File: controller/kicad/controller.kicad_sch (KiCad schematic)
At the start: 33 parts, among them J1 pcie_98, J2 USB_C_Receptacle_USB2.0, U1 WeAct_STM32H750_Module, U10 ESD5344D, U11 ESD5344D, U12 ESD5344D, U13 ESD5344D, U14 ESD5344D, U15 ESD5344D, U16 CP2102N-A01-GQFN28-Interface_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, U2 ESD5344D, U3 ESD5344D, U4 ESD5344D, U5 ESD5344D, U6 ESD5344D, U7 ESD5344D, U8 ESD5344D, U9 ESD5344D

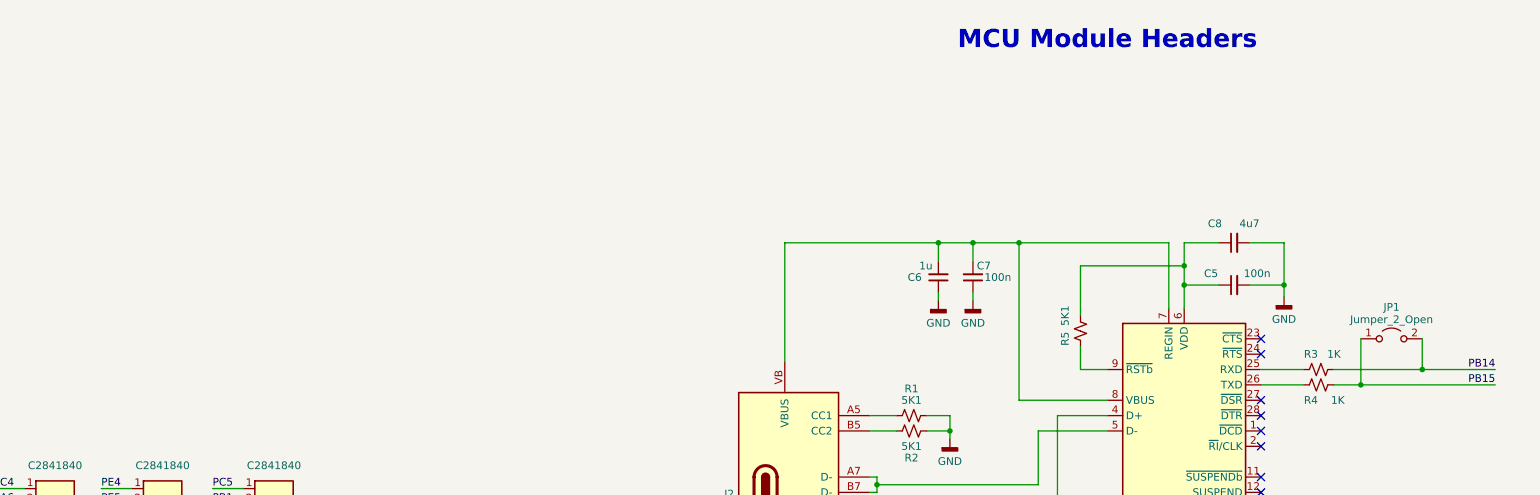
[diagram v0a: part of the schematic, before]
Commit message: Updated the Controller's schematic to reflect the new RX/TX pin of the datalink serial link.
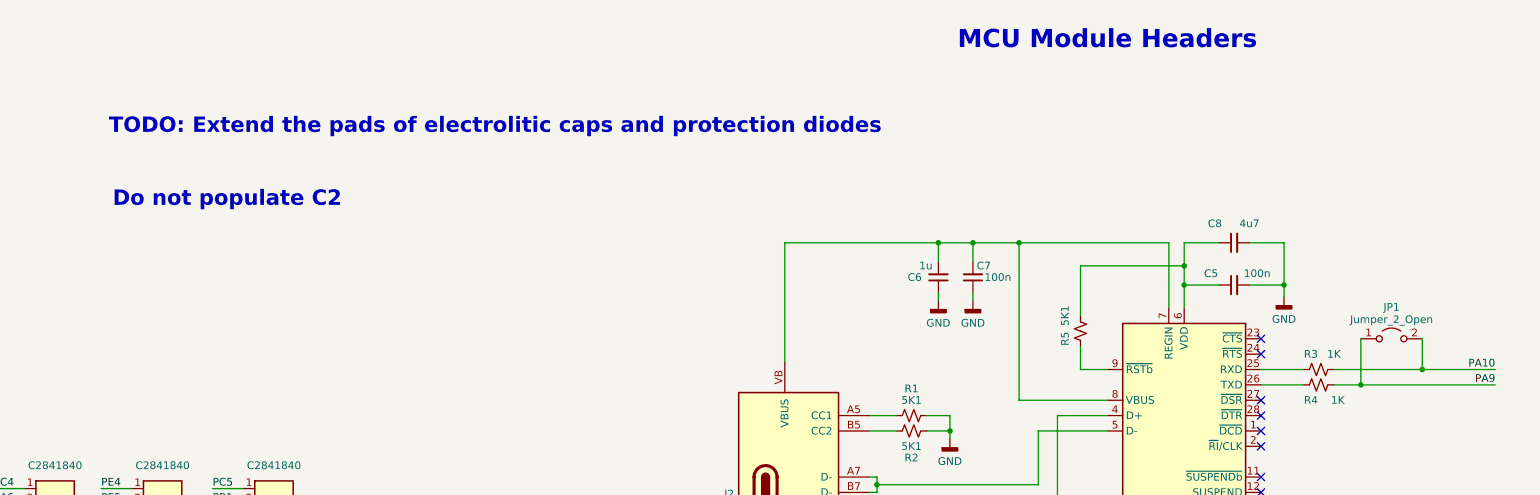
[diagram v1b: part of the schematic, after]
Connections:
- net PA10: now also JP1.2 (B), R3.2
- net PA9: now also JP1.1 (A), R4.2
- net PB14: no longer JP1.2 (B), R3.2
- net PB15: no longer JP1.1 (A), R4.2
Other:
- note added: "Do not populate C2"
- note added: "TODO: Extend the pads of electrolitic caps and protection diodes"
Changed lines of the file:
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@@
     (effects (font (size 3 3) (thickness 0.6) bold) (justify left bottom))
+  )
+  (text "TODO: Extend the pads of electrolitic caps and protection diodes"
+    (at 138.43 140.335 0)
+    (effects (font (size 2.54 2.54) (thickness 0.508) bold (color 255 0 0 1)) (justify left bottom))
   )
   (text "MCU Module Headers" (at 278.765 126.365 0)
@@
   (text "Edge Connector" (at 32.385 105.41 0)
     (effects (font (size 3 3) (thickness 0.6) bold) (justify left bottom))
+  )
+  (text "Do not populate C2" (at 139.065 152.4 0)
+    (effects (font (size 2.54 2.54) (thickness 0.508) bold (color 255 0 0 1)) (justify left bottom))
   )
   (text "POWER" (at 170.18 106.68 0)
@@
     (effects (font (size 1.27 1.27)) (justify left bottom))
   )
-  (label "PB15" (at 367.665 181.61 180) (fields_autoplaced)
+  (label "PA9" (at 367.665 181.61 180) (fields_autoplaced)
     (effects (font (size 1.27 1.27)) (justify right bottom))
   )
@@
     (effects (font (size 1.27 1.27)) (justify right bottom))
   )
-  (label "PB14" (at 367.665 179.07 180) (fields_autoplaced)
-    (effects (font (size 1.27 1.27)) (justify right bottom))
-  )
+  (label "PA10" (at 367.665 179.07 180) (fields_autoplaced)
+    (effects (font (size 1.27 1.27)) (justify right bottom))
+  )

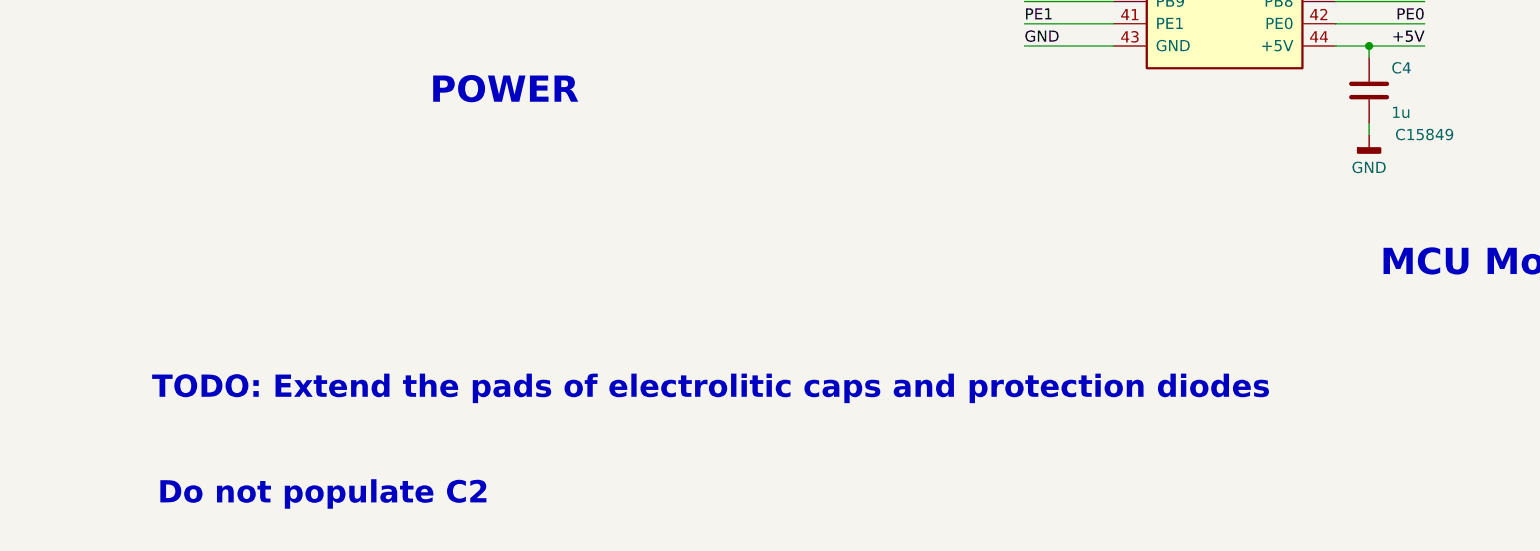
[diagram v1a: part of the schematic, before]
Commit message: Added comments to the Backplane schematic.
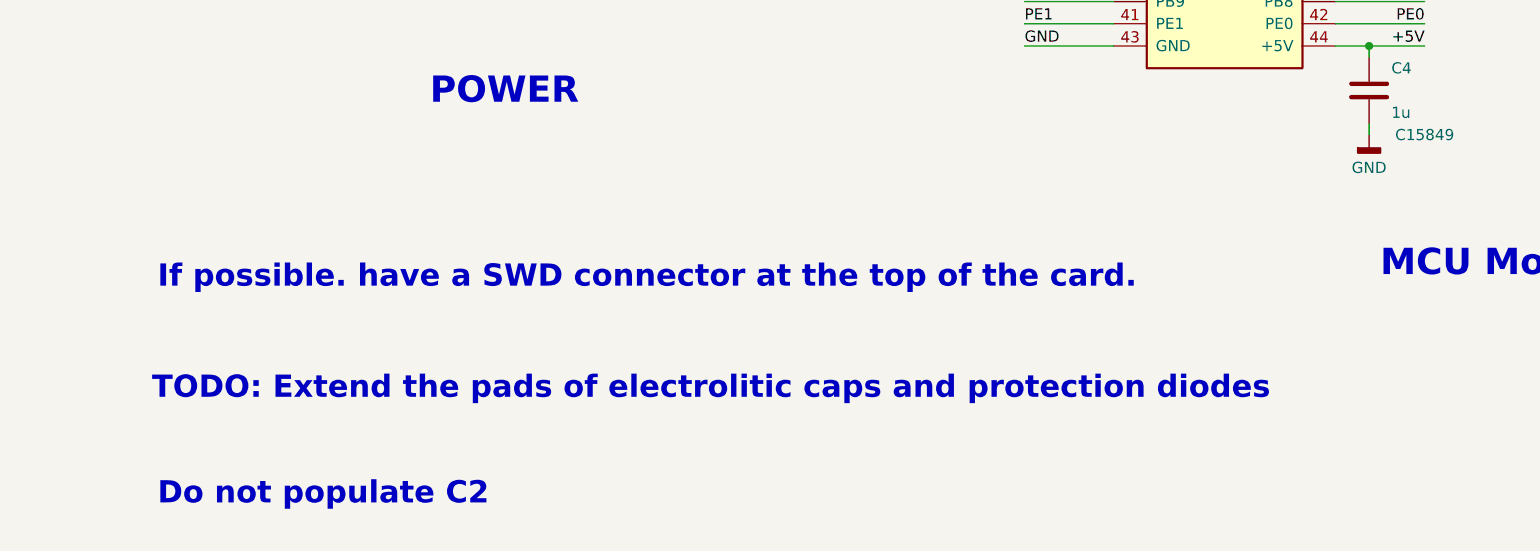
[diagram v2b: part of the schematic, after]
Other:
- note added: "If possible. have a SWD connector at the top of the card."
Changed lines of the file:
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@@
+    (effects (font (size 2.54 2.54) (thickness 0.508) bold (color 255 0 0 1)) (justify left bottom))
+  )
+  (text "If possible. have a SWD connector at the top of the card."
+    (at 139.065 127.635 0)
     (effects (font (size 2.54 2.54) (thickness 0.508) bold (color 255 0 0 1)) (justify left bottom))
   )

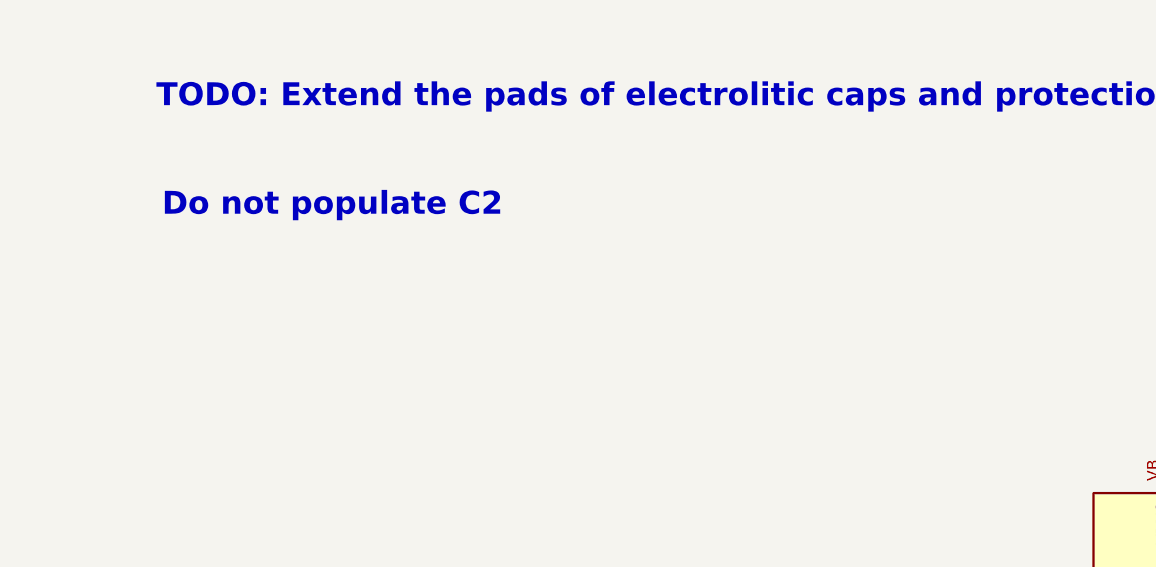
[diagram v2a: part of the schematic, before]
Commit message: Added a comment to the controller's schematic.
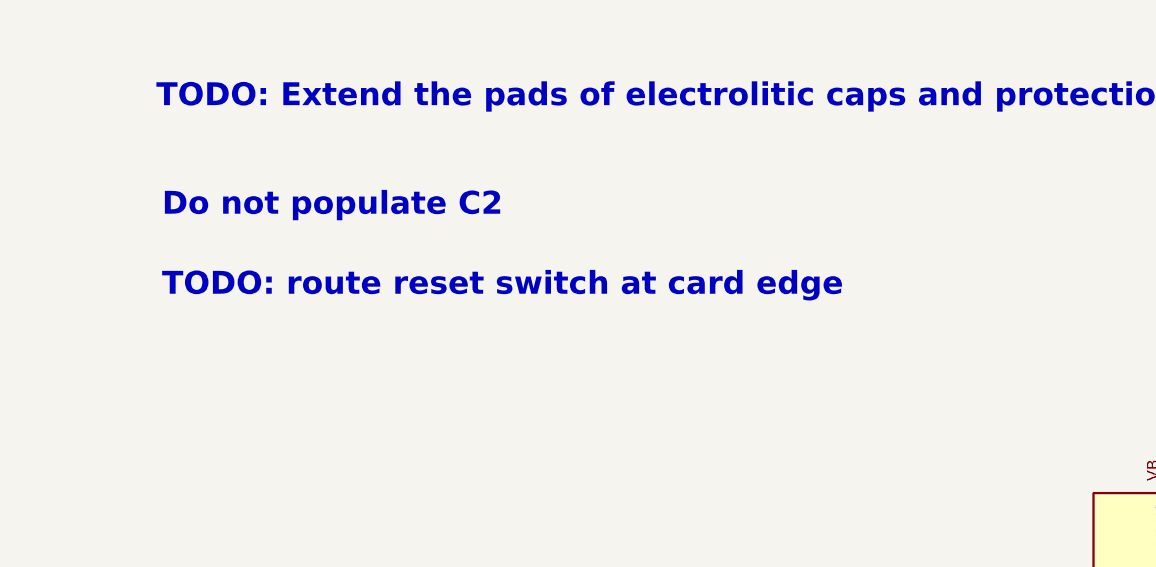
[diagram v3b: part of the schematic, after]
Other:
- note added: "TODO: route reset switch at card edge"
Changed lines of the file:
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@@
     (effects (font (size 3 3) (thickness 0.6) bold) (justify left bottom))
+  )
+  (text "TODO: route reset switch at card edge" (at 139.065 161.29 0)
+    (effects (font (size 2.54 2.54) (thickness 0.508) bold (color 255 0 0 1)) (justify left bottom))
   )
   (label "PB11" (at 112.395 119.38 180) (fields_autoplaced)

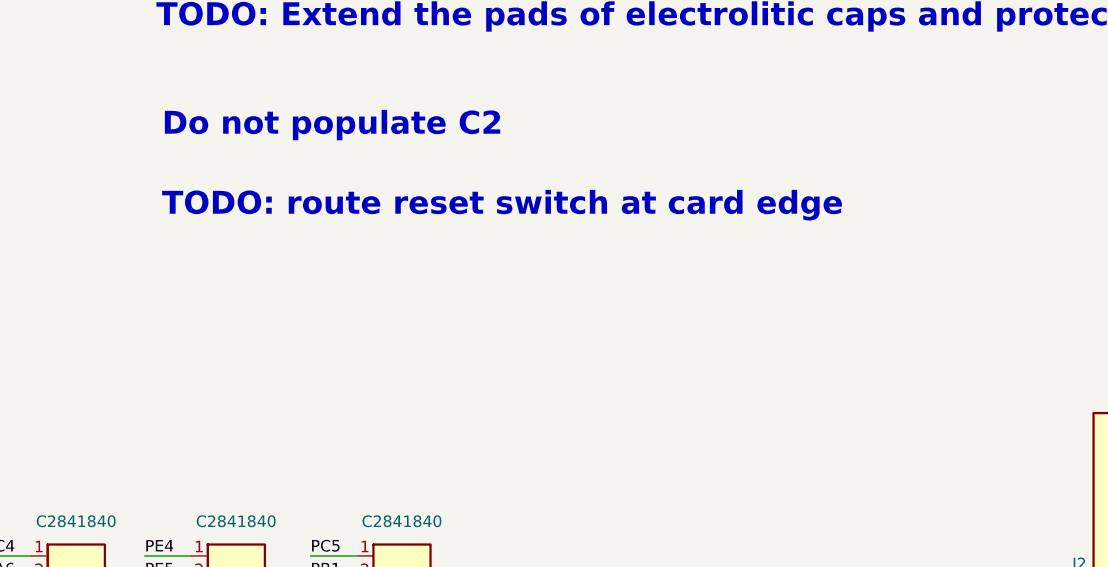
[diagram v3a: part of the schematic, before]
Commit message: Progressing on the ADC layout.
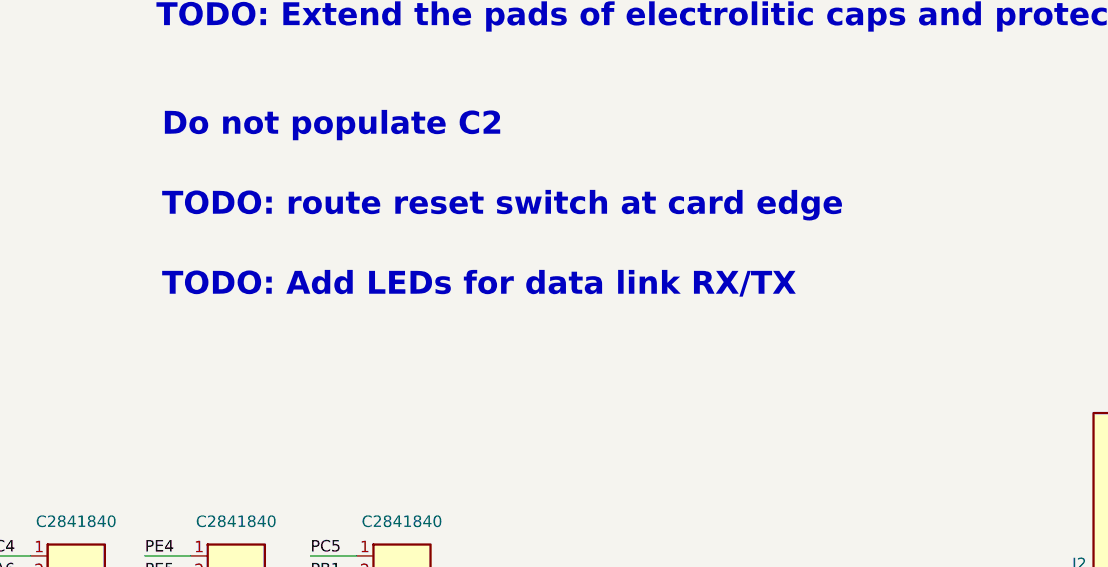
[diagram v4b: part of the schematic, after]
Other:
- note added: "TODO: Add LEDs for data link RX/TX"
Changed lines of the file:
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@@
     (effects (font (size 3 3) (thickness 0.6) bold) (justify left bottom))
+  )
+  (text "TODO: Add LEDs for data link RX/TX" (at 139.065 170.18 0)
+    (effects (font (size 2.54 2.54) (thickness 0.508) bold (color 255 0 0 1)) (justify left bottom))
   )
   (text "Edge Connector" (at 32.385 105.41 0)

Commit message: Added a reset button to the controller's schematic.
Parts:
- added SW1: SW_MEC_5E, symbol Switch:SW_MEC_5E
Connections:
- net GND: now also SW1.1, SW1.2
- net NRST: now reaches U1.80 (NRST)
- net NRST: now also SW1.3 (K), SW1.4 (A)
- no-connect marks 81 -> 80
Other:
- note added: "TODO: Do not populate C2"
- note added: "TODO: If possible. have a SWD connector at the top of the card."
- note removed: "Do not populate C2"
- note removed: "If possible. have a SWD connector at the top of the card."
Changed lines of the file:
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@@
   (junction (at 86.995 38.1) (diameter 0) (color 0 0 0 0)
   )
+  (junction (at 354.965 120.65) (diameter 0) (color 0 0 0 0)
+  )
   (junction (at 83.185 38.1) (diameter 0) (color 0 0 0 0)
   )
+  (junction (at 354.965 133.35) (diameter 0) (color 0 0 0 0)
+  )
   (junction (at 277.495 189.23) (diameter 0) (color 0 0 0 0)
   )
@@
   (junction (at 86.995 40.64) (diameter 0) (color 0 0 0 0)
   )
-  (no_connect (at 344.805 89.535))
   (no_connect (at 89.535 160.02))
   (no_connect (at 89.535 152.4))
@@
   (no_connect (at 273.685 56.515))
   (no_connect (at 102.235 129.54))
+  (wire (pts (xy 354.965 132.08) (xy 354.965 133.35))
+    (stroke (width 0) (type default))
+  )
   (wire (pts (xy 102.235 88.9) (xy 112.395 88.9))
     (stroke (width 0) (type default))
@@
     (stroke (width 0) (type default))
   )
+  (wire (pts (xy 347.98 118.11) (xy 354.965 118.11))
+    (stroke (width 0) (type default))
+  )
   (wire (pts (xy 86.995 43.18) (xy 89.535 43.18))
     (stroke (width 0) (type default))
@@
     (stroke (width 0) (type default))
   )
+  (wire (pts (xy 354.965 133.35) (xy 354.965 135.255))
+    (stroke (width 0) (type default))
+  )
+  (wire (pts (xy 357.505 133.35) (xy 354.965 133.35))
+    (stroke (width 0) (type default))
+  )
   (wire (pts (xy 79.375 73.66) (xy 89.535 73.66))
     (stroke (width 0) (type default))
@@
     (stroke (width 0) (type default))
   )
+  (wire (pts (xy 357.505 121.92) (xy 357.505 120.65))
+    (stroke (width 0) (type default))
+  )
   (wire (pts (xy 355.6 179.07) (xy 367.665 179.07))
     (stroke (width 0) (type default))
@@
     (stroke (width 0) (type default))
   )
+  (wire (pts (xy 357.505 120.65) (xy 354.965 120.65))
+    (stroke (width 0) (type default))
+  )
   (wire (pts (xy 66.04 198.755) (xy 71.12 198.755))
     (stroke (width 0) (type default))
@@
     (stroke (width 0) (type default))
   )
+  (wire (pts (xy 354.965 120.65) (xy 354.965 118.11))
+    (stroke (width 0) (type default))
+  )
   (wire (pts (xy 332.74 158.115) (xy 332.74 165.1))
     (stroke (width 0) (type default))
@@
     (stroke (width 0) (type default))
   )
+  (wire (pts (xy 344.805 89.535) (xy 354.965 89.535))
+    (stroke (width 0) (type default))
+  )
   (wire (pts (xy 277.495 186.69) (xy 277.495 189.23))
     (stroke (width 0) (type default))
@@
     (stroke (width 0) (type default))
   )
+  (wire (pts (xy 357.505 132.08) (xy 357.505 133.35))
+    (stroke (width 0) (type default))
+  )
   (wire (pts (xy 288.925 158.115) (xy 313.69 158.115))
     (stroke (width 0) (type default))
@@
     (stroke (width 0) (type default))
   )
+  (wire (pts (xy 354.965 121.92) (xy 354.965 120.65))
+    (stroke (width 0) (type default))
+  )
   (wire (pts (xy 316.23 158.115) (xy 316.23 161.925))
     (stroke (width 0) (type default))
@@
   )
   (text "TODO: Extend the pads of electrolitic caps and protection diodes"
-    (at 138.43 140.335 0)
+    (at 138.43 139.065 0)
     (effects (font (size 2.54 2.54) (thickness 0.508) bold (color 255 0 0 1)) (justify left bottom))
   )
@@
     (effects (font (size 3 3) (thickness 0.6) bold) (justify left bottom))
   )
-  (text "Do not populate C2" (at 139.065 152.4 0)
+  (text "TODO: Do not populate C2" (at 139.065 149.86 0)
     (effects (font (size 2.54 2.54) (thickness 0.508) bold (color 255 0 0 1)) (justify left bottom))
   )
-  (text "If possible. have a SWD connector at the top of the card."
+  (text "TODO: If possible. have a SWD connector at the top of the card."
     (at 139.065 127.635 0)
     (effects (font (size 2.54 2.54) (thickness 0.508) bold (color 255 0 0 1)) (justify left bottom))
@@
     (effects (font (size 3 3) (thickness 0.6) bold) (justify left bottom))
   )
-  (text "TODO: route reset switch at card edge" (at 139.065 161.29 0)
+  (text "TODO: route reset switch at card edge" (at 139.065 159.385 0)
     (effects (font (size 2.54 2.54) (thickness 0.508) bold (color 255 0 0 1)) (justify left bottom))
   )
@@
     (effects (font (size 1.27 1.27)) (justify right bottom))
   )
+  (label "NRST" (at 354.965 89.535 180) (fields_autoplaced)
+    (effects (font (size 1.27 1.27)) (justify right bottom))
+  )
   (label "+5V" (at 283.845 99.695 180) (fields_autoplaced)
     (effects (font (size 1.27 1.27)) (justify right bottom))
@@
     (effects (font (size 1.27 1.27)) (justify left bottom))
   )
+  (label "NRST" (at 347.98 118.11 0) (fields_autoplaced)
+    (effects (font (size 1.27 1.27)) (justify left bottom))
+  )
   (label "PB8" (at 79.375 71.12 0) (fields_autoplaced)
     (effects (font (size 1.27 1.27)) (justify left bottom))
@@
     )
   )
+  (symbol (lib_id "Switch:SW_MEC_5E") (at 357.505 127 90) (unit 1)
+    (in_bom yes) (on_board yes) (dnp no) (fields_autoplaced)
+    (property "Reference" "SW1" (at 358.14 126.365 90)
+      (effects (font (size 1.27 1.27)) (justify right))
+    )
+    (property "Value" "SW_MEC_5E" (at 358.14 128.905 90)
+      (effects (font (size 1.27 1.27)) (justify right))
+    )
+    (property "Footprint" "" (at 349.885 127 0)
+      (effects (font (size 1.27 1.27)) hide)
+    )
+    (property "Datasheet" "http://www.apem.com/int/index.php?controller=attachment&id_attachment=1371" (at 349.885 127 0)
+      (effects (font (size 1.27 1.27)) hide)
+    )
+    (pin "1")
+    (pin "2")
+    (pin "3")
+    (pin "4")
+    (instances
+      (project "controller"
+        (path "/0dcd9c8c-bd5a-437f-856e-101fb6cf8b66"
+          (reference "SW1") (unit 1)
+        )
+      )
+    )
+  )
   (symbol (lib_id "common:GND") (at 165.735 211.455 0) (unit 1)
     (in_bom yes) (on_board yes) (dnp no) (fields_autoplaced)
@@
         )
       )
+    )
+  )
+  (symbol (lib_id "common:GND") (at 354.965 135.255 0) (unit 1)
+    (in_bom yes) (on_board yes) (dnp no) (fields_autoplaced)
+    (property "Reference" "#PWR026" (at 354.965 141.605 0)
+      (effects (font (size 1.27 1.27)) hide)
+    )
+    (property "Value" "GND" (at 354.965 139.0095 0)
+      (effects (font (size 1.27 1.27)))
+    )
+    (property "Footprint" "" (at 354.965 135.255 0)
+      (effects (font (size 1.27 1.27)) hide)
+    )
+    (property "Datasheet" "" (at 354.965 135.255 0)
+      (effects (font (size 1.27 1.27)) hide)
+    )
+    (pin "1")
+    (instances
+      (project "controller"
+        (path "/0dcd9c8c-bd5a-437f-856e-101fb6cf8b66"
+          (reference "#PWR026") (unit 1)
+        )
+      )
